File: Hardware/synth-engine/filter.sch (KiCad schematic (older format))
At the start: 34 parts

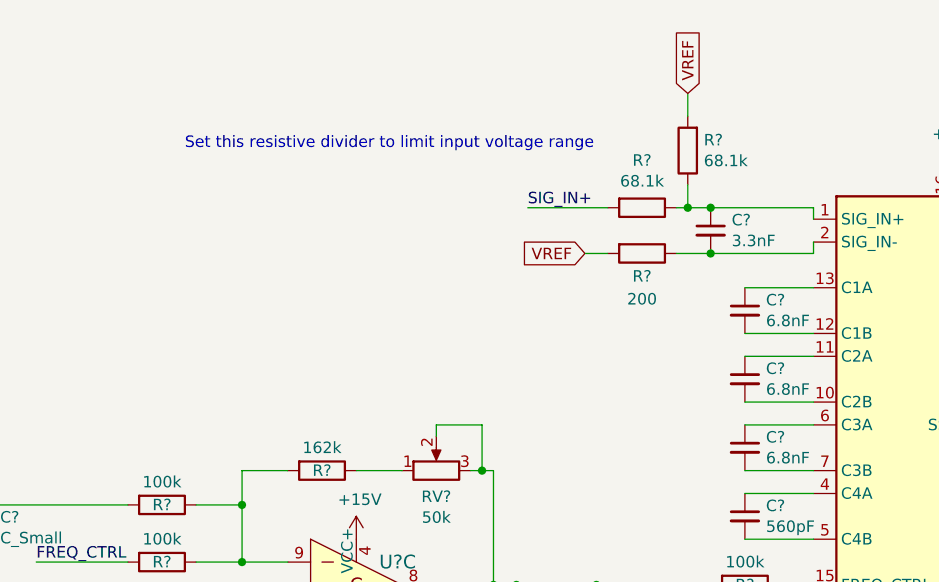
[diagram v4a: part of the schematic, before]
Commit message: add LFP following DAC diff outputs and connect DAC output to VCF input
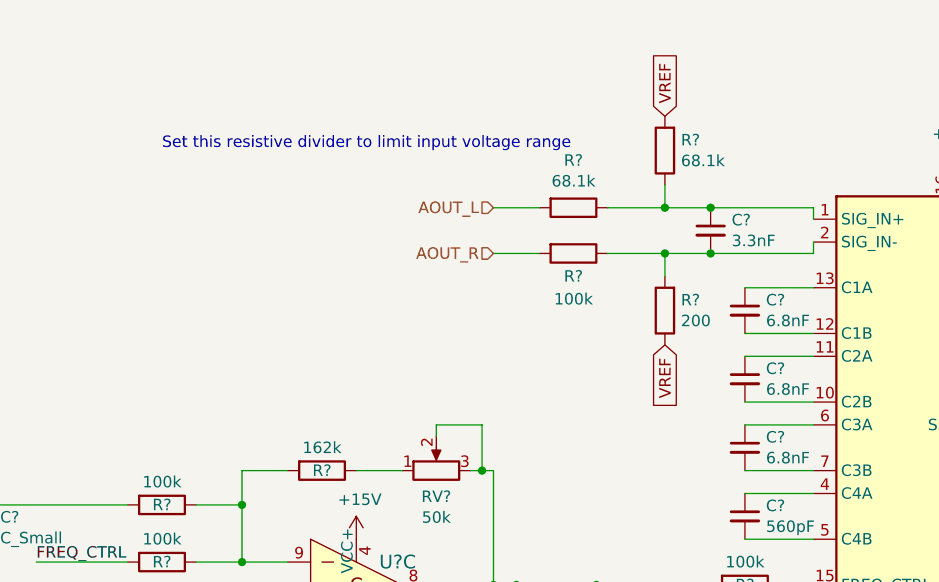
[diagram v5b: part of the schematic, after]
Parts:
- added R?: 200, symbol Device:R
- R?: value 200 -> 100k
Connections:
- net VREF: now also R?.1; no longer R?.2
- net at C?.2, R?.1, U?.2 (SIG_IN-): now also R?.2
- net SIG_IN+ renamed AOUT_L
- new net AOUT_R: R?.2
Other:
- moved on the sheet: R?
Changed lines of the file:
@@
 L Device:R R?
 U 1 1 5DD462EE
-P 5050 2650
-F 0 "R?" V 4843 2650 50  0000 C CNN
-F 1 "68.1k" V 4934 2650 50  0000 C CNN
-F 2 "" V 4980 2650 50  0001 C CNN
-F 3 "~" H 5050 2650 50  0001 C CNN
-	1    5050 2650
+P 4750 2650
+F 0 "R?" V 4543 2650 50  0000 C CNN
+F 1 "68.1k" V 4634 2650 50  0000 C CNN
+F 2 "" V 4680 2650 50  0001 C CNN
+F 3 "~" H 4750 2650 50  0001 C CNN
+	1    4750 2650
 	0    1    1    0
 $EndComp
@@
 L Device:R R?
 U 1 1 5DD47650
-P 5050 2850
-F 0 "R?" V 5150 2850 50  0000 C CNN
-F 1 "200" V 5250 2850 50  0000 C CNN
-F 2 "" V 4980 2850 50  0001 C CNN
-F 3 "~" H 5050 2850 50  0001 C CNN
-	1    5050 2850
-	0    1    1    0
-$EndComp
-Wire Wire Line
-	5200 2850 5350 2850
+P 4750 2850
+F 0 "R?" V 4850 2850 50  0000 C CNN
+F 1 "100k" V 4950 2850 50  0000 C CNN
+F 2 "" V 4680 2850 50  0001 C CNN
+F 3 "~" H 4750 2850 50  0001 C CNN
+	1    4750 2850
+	0    1    1    0
+$EndComp
+Wire Wire Line
+	4900 2850 5150 2850
 Connection ~ 5350 2850
-Wire Wire Line
-	5200 2650 5250 2650
 Connection ~ 5350 2650
-Text Label 4550 2650 0    50   ~ 0
-SIG_IN+
-Wire Wire Line
-	4550 2650 4900 2650
 $Comp
 L dk_Linear-Amplifiers-Instrumentation-OP-Amps-Buffer-Amps:TL074CN U?
@@
 Wire Wire Line
 	2400 4200 2800 4200
-Text GLabel 4800 2850 0    50   Input ~ 0
-VREF
-Wire Wire Line
-	4800 2850 4900 2850
 Text GLabel 5750 5150 3    50   Input ~ 0
 VREF
 Wire Wire Line
 	5750 5150 5750 5000
-Text GLabel 5250 2150 1    50   Input ~ 0
+Text GLabel 5150 2250 1    50   Input ~ 0
 VREF
 $Comp
 L Device:R R?
 U 1 1 5DD74FCF
-P 5250 2400
-F 0 "R?" H 5180 2354 50  0000 R CNN
-F 1 "68.1k" H 5180 2445 50  0000 R CNN
-F 2 "" V 5180 2400 50  0001 C CNN
-F 3 "~" H 5250 2400 50  0001 C CNN
-	1    5250 2400
+P 5150 2400
+F 0 "R?" H 5080 2354 50  0000 R CNN
+F 1 "68.1k" H 5080 2445 50  0000 R CNN
+F 2 "" V 5080 2400 50  0001 C CNN
+F 3 "~" H 5150 2400 50  0001 C CNN
+	1    5150 2400
 	-1   0    0    1
 $EndComp
-Wire Wire Line
-	5250 2550 5250 2650
-Connection ~ 5250 2650
-Wire Wire Line
-	5250 2650 5350 2650
-Wire Wire Line
-	5250 2150 5250 2250
-Text Notes 3050 2400 0    50   ~ 0
+Text Notes 2950 2400 0    50   ~ 0
 Set this resistive divider to limit input voltage range
 $Comp
@@
 Text Label 2500 5650 0    50   ~ 0
 Q_CTRL
+$Comp
+L Device:R R?
+U 1 1 5DE8132C
+P 5150 3100
+F 0 "R?" H 5080 3054 50  0000 R CNN
+F 1 "200" H 5080 3145 50  0000 R CNN
+F 2 "" V 5080 3100 50  0001 C CNN
+F 3 "~" H 5150 3100 50  0001 C CNN
+	1    5150 3100
+	-1   0    0    1
+$EndComp
+Wire Wire Line
+	5150 2950 5150 2850
+Connection ~ 5150 2850
+Wire Wire Line
+	5150 2850 5350 2850
+Text GLabel 5150 3250 3    50   Input ~ 0
+VREF
+Text HLabel 4400 2650 0    50   Input ~ 0
+AOUT_L
+Text HLabel 4400 2850 0    50   Input ~ 0
+AOUT_R
+Wire Wire Line
+	4400 2650 4600 2650
+Wire Wire Line
+	4600 2850 4400 2850
+Wire Wire Line
+	4900 2650 5150 2650
+Wire Wire Line
+	5150 2550 5150 2650
+Connection ~ 5150 2650
+Wire Wire Line
+	5150 2650 5350 2650
 $EndSCHEMATC

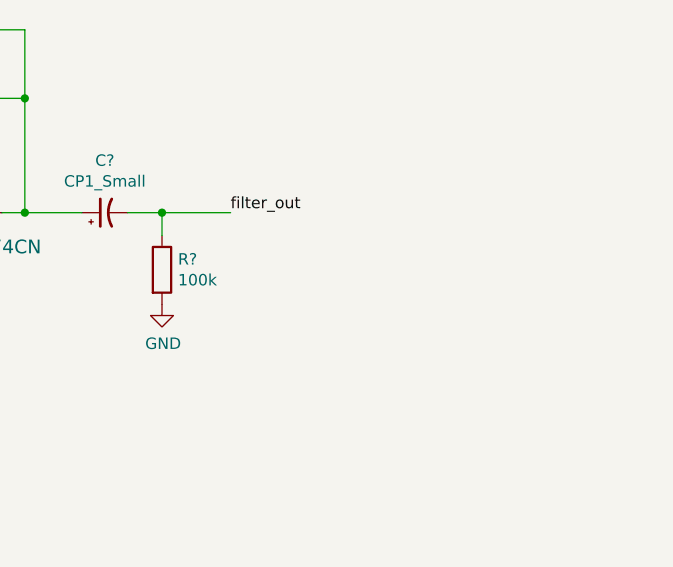
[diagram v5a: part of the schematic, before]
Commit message: add filtering in front of 3.3V regulators
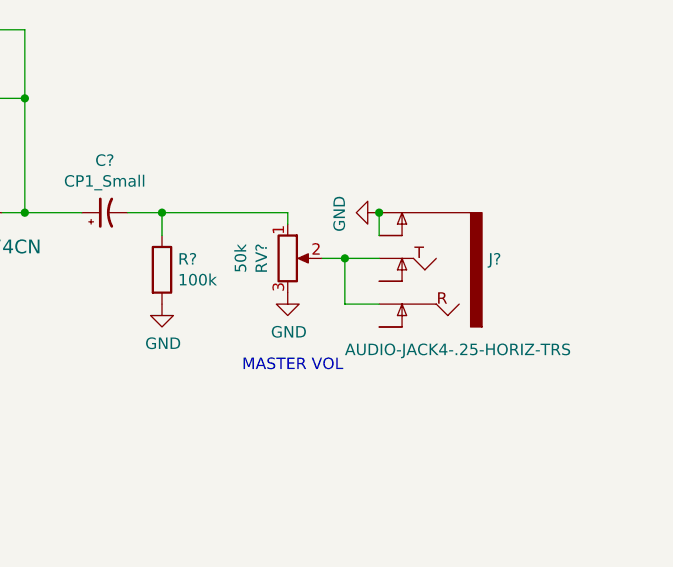
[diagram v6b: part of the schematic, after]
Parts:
- added J?: AUDIO-JACK4-.25-HORIZ-TRS, AUDIO-JACK-.25-INCH-HORIZ-PTH, symbol SparkFun-Connectors:AUDIO-JACK4-.25-HORIZ-TRS
- added RV?: 50k, symbol Device:R_POT
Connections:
- net GND: now also J?.SLEE (EARTH-NORM), RV?.3
- net filter_out: no longer names the net of C?.2, R?.1
- net filter_out: now also RV?.1
- new net: J?.RING (RING-NORM), J?.TIP, RV?.2
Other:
- note added: "MASTER VOL"
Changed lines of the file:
@@
 Wire Wire Line
 	8950 3800 8950 3700
-Connection ~ 8950 3700
-Wire Wire Line
-	8950 3700 9250 3700
 $Comp
 L power:GND #PWR?
@@
 	1    0    0    -1
 $EndComp
-Text Label 9250 3700 0    50   ~ 0
-filter_out
 $Comp
 L power:+15V #PWR?
@@
 Wire Wire Line
 	5150 2650 5350 2650
+$Comp
+L SparkFun-Connectors:AUDIO-JACK4-.25-HORIZ-TRS J?
+U 1 1 5DE9AC5B
+P 10100 4000
+F 0 "J?" H 9822 4096 50  0000 R CNN
+F 1 "AUDIO-JACK4-.25-HORIZ-TRS" H 10450 3700 50  0000 R CNN
+F 2 "AUDIO-JACK-.25-INCH-HORIZ-PTH" H 10130 4150 20  0001 C CNN
+F 3 "" H 10100 4000 60  0000 C CNN
+	1    10100 4000
+	-1   0    0    -1
+$EndComp
+$Comp
+L power:GND #PWR?
+U 1 1 5DE9C6F0
+P 9900 3700
+F 0 "#PWR?" H 9900 3450 50  0001 C CNN
+F 1 "GND" H 9905 3527 50  0000 C CNN
+F 2 "" H 9900 3700 50  0001 C CNN
+F 3 "" H 9900 3700 50  0001 C CNN
+	1    9900 3700
+	0    1    1    0
+$EndComp
+Wire Wire Line
+	9900 3800 9900 3700
+Connection ~ 9900 3700
+$Comp
+L Device:R_POT RV?
+U 1 1 5DEA599F
+P 9500 3900
+F 0 "RV?" V 9386 3900 50  0000 C CNN
+F 1 "50k" V 9295 3900 50  0000 C CNN
+F 2 "" H 9500 3900 50  0001 C CNN
+F 3 "~" H 9500 3900 50  0001 C CNN
+	1    9500 3900
+	1    0    0    -1
+$EndComp
+Wire Wire Line
+	9500 3750 9500 3700
+Wire Wire Line
+	9500 3700 8950 3700
+Connection ~ 8950 3700
+$Comp
+L power:GND #PWR?
+U 1 1 5DEA9190
+P 9500 4050
+F 0 "#PWR?" H 9500 3800 50  0001 C CNN
+F 1 "GND" H 9505 3877 50  0000 C CNN
+F 2 "" H 9500 4050 50  0001 C CNN
+F 3 "" H 9500 4050 50  0001 C CNN
+	1    9500 4050
+	1    0    0    -1
+$EndComp
+Wire Wire Line
+	9900 3900 9750 3900
+Wire Wire Line
+	9750 3900 9750 4100
+Wire Wire Line
+	9750 4100 9900 4100
+Connection ~ 9750 3900
+Wire Wire Line
+	9750 3900 9650 3900
+Text Notes 9300 4400 0    50   ~ 0
+MASTER VOL
 $EndSCHEMATC

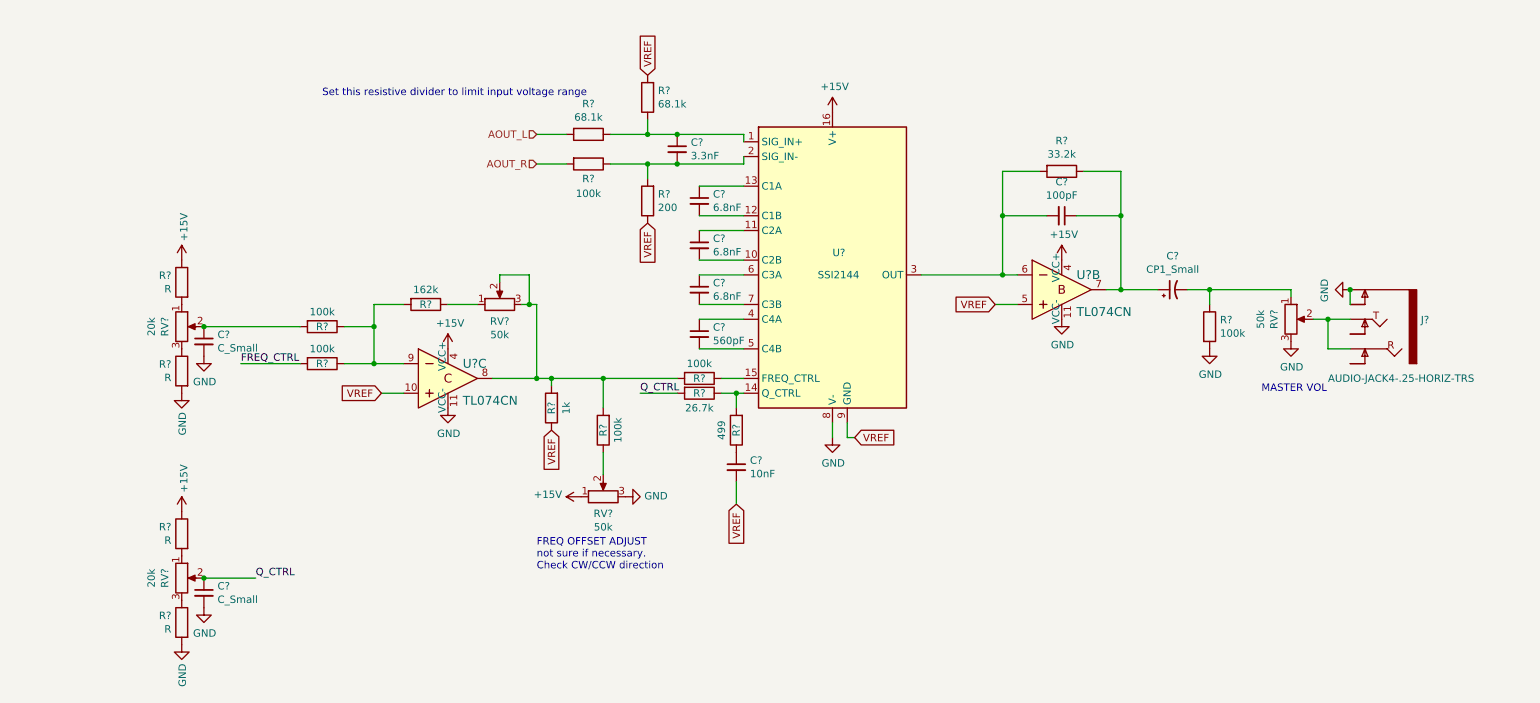
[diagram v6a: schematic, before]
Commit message: assign footprints to schematic symbols.
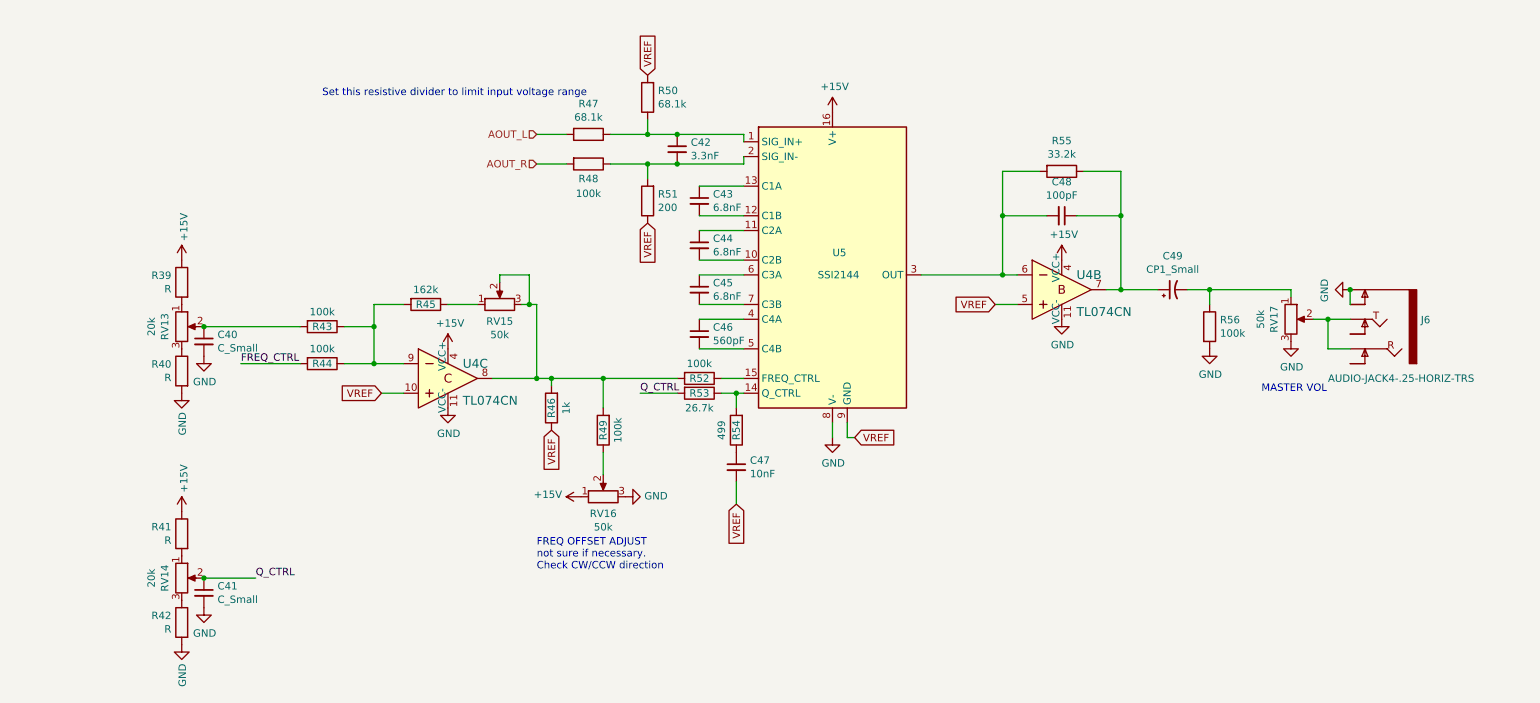
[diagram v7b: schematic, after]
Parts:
- C40, C41, C42, C43, C44, C45, C46, C47, C48: renamed from C?; footprint (none) -> SparkFun-Passives:0805
- C49: renamed from C?; footprint (none) -> Capacitor_SMD:CP_Elec_6.3x5.4
- J6: renamed from J?; footprint AUDIO-JACK-.25-INCH-HORIZ-PTH -> SparkFun-Connectors:AUDIO-JACK-.25-INCH-HORIZ-PTH
- R39, R40, R41, R42, R43, R44, R45, R46, R47, R48, R49, R50, R51, R52, R53, R54, R55, R56: renamed from R?; footprint (none) -> SparkFun-Passives:0805
- RV13, RV14, RV15, RV16, RV17: renamed from RV?; footprint (none) -> Potentiometer_THT:Potentiometer_Alps_RK09K_Single_Vertical
- gave numbers to parts that had none: 2
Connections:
- net at J6.RING (RING-NORM): now also J6.TIP, RV17.2

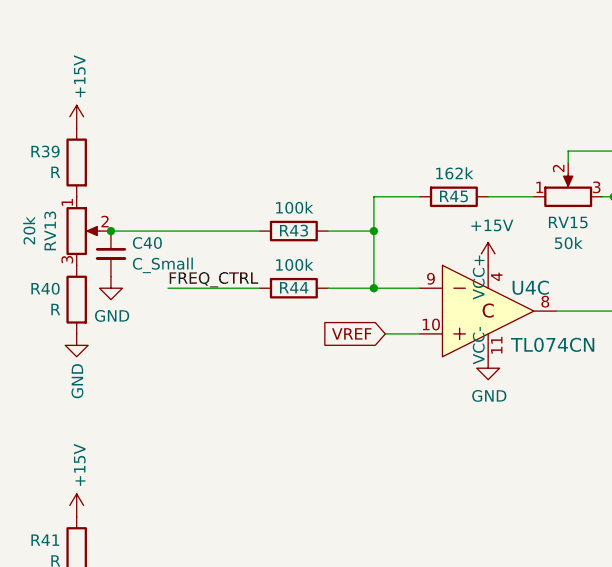
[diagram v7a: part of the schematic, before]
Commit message: rough placement and symbol organization. If I need to start PCB layout over from scracth, revert to this commit.
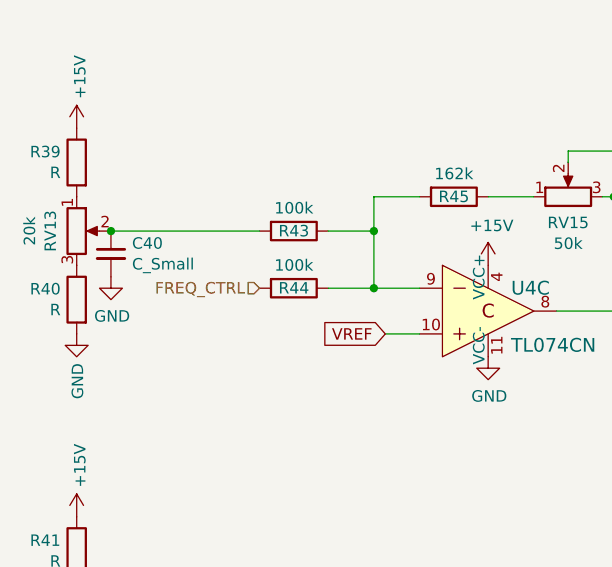
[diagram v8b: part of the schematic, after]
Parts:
- U4: footprint digikey-footprints:DIP-14_W3mm -> SparkFun-AnalogIC:SOIC8
- U5: footprint Package_SO:SSOP-16_3.9x4.9mm_P0.635mm -> SparkFun-AnalogIC:SSOP16
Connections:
- net at J6.RING (RING-NORM): now also J6.TIP, RV17.2
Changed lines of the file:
@@
 F 0 "U5" H 6400 3750 50  0000 L CNN
 F 1 "SSI2144" H 6300 3600 50  0000 L CNN
-F 2 "Package_SO:SSOP-16_3.9x4.9mm_P0.635mm" H 7300 3500 50  0001 C CNN
+F 2 "SparkFun-AnalogIC:SSOP16" H 7300 3500 50  0001 C CNN
 F 3 "http://www.soundsemiconductor.com/downloads/ssi2144datasheet.pdf" H 7100 3350 50  0001 C CNN
 	1    6400 3600
@@
 F 0 "U4" H 8050 3800 60  0000 L CNN
 F 1 "TL074CN" H 8050 3550 60  0000 L CNN
-F 2 "digikey-footprints:DIP-14_W3mm" H 8150 3900 60  0001 L CNN
+F 2 "SparkFun-AnalogIC:SOIC8" H 8150 3900 60  0001 L CNN
 F 3 "http://www.ti.com/lit/ds/symlink/tl071a.pdf" H 8150 4000 60  0001 L CNN
 F 4 "296-1777-5-ND" H 8150 4100 60  0001 L CNN "Digi-Key_PN"
@@
 F 0 "U4" H 3900 4400 60  0000 L CNN
 F 1 "TL074CN" H 3900 4150 60  0000 L CNN
-F 2 "digikey-footprints:DIP-14_W3mm" H 4000 4500 60  0001 L CNN
+F 2 "SparkFun-AnalogIC:SOIC8" H 4000 4500 60  0001 L CNN
 F 3 "http://www.ti.com/lit/ds/symlink/tl071a.pdf" H 4000 4600 60  0001 L CNN
 F 4 "296-1777-5-ND" H 4000 4700 60  0001 L CNN "Digi-Key_PN"
@@
 Wire Wire Line
 	5100 4400 5350 4400
-Text Label 2400 4200 0    50   ~ 0
-FREQ_CTRL
-Wire Wire Line
-	2400 4200 2800 4200
 Text GLabel 5750 5150 3    50   Input ~ 0
 VREF
@@
 Text Notes 9300 4400 0    50   ~ 0
 MASTER VOL
+Text HLabel 2800 4200 0    50   Input ~ 0
+FREQ_CTRL
 $EndSCHEMATC
